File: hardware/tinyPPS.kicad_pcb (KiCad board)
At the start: 2 copper layers, 60 x 40 mm, 65 parts, among them IC1 AP2205-33Y-13, IC2 AP33772SDKZ-13-FA01, J1 USB_C_Receptacle_USB2.0_14P, J2 187-3802, J3 187-3802, J5 SM03B-SRSS-TB_LF__SN_, Q1 DMN3009SFG-7, Q2 DMN3009SFG-7, Q3 BSS123, Q4 BSS123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

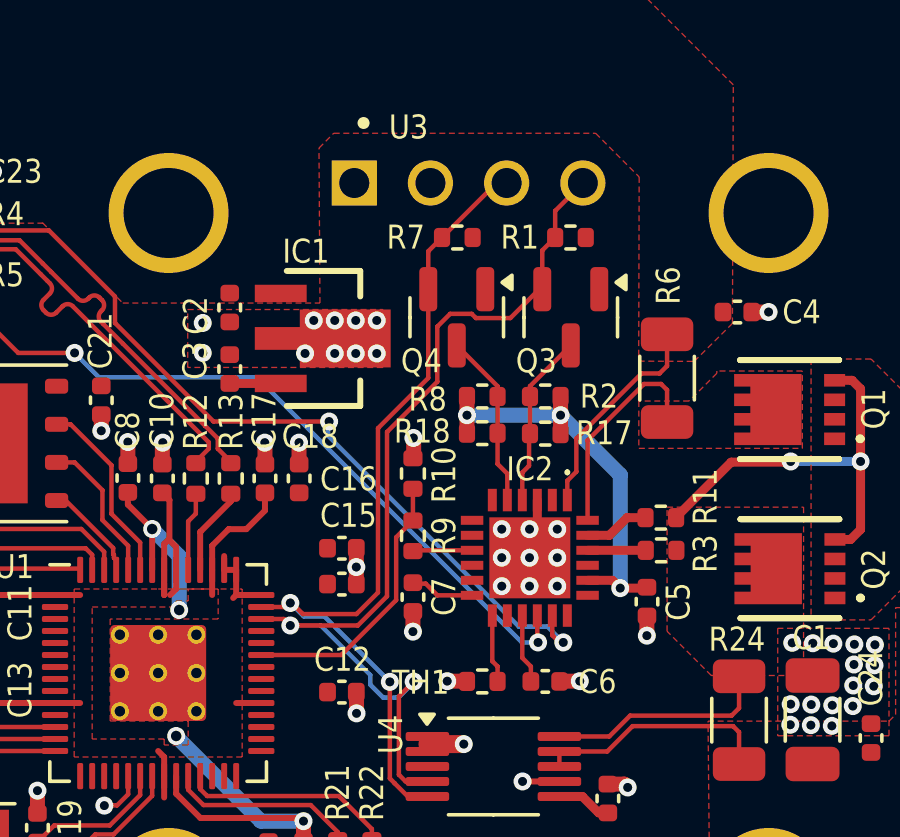
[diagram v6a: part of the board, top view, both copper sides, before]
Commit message: Schematic: Remove i2c level shifters
AP33772s' i2c can operate at 3V3, there is no need for level shifters.
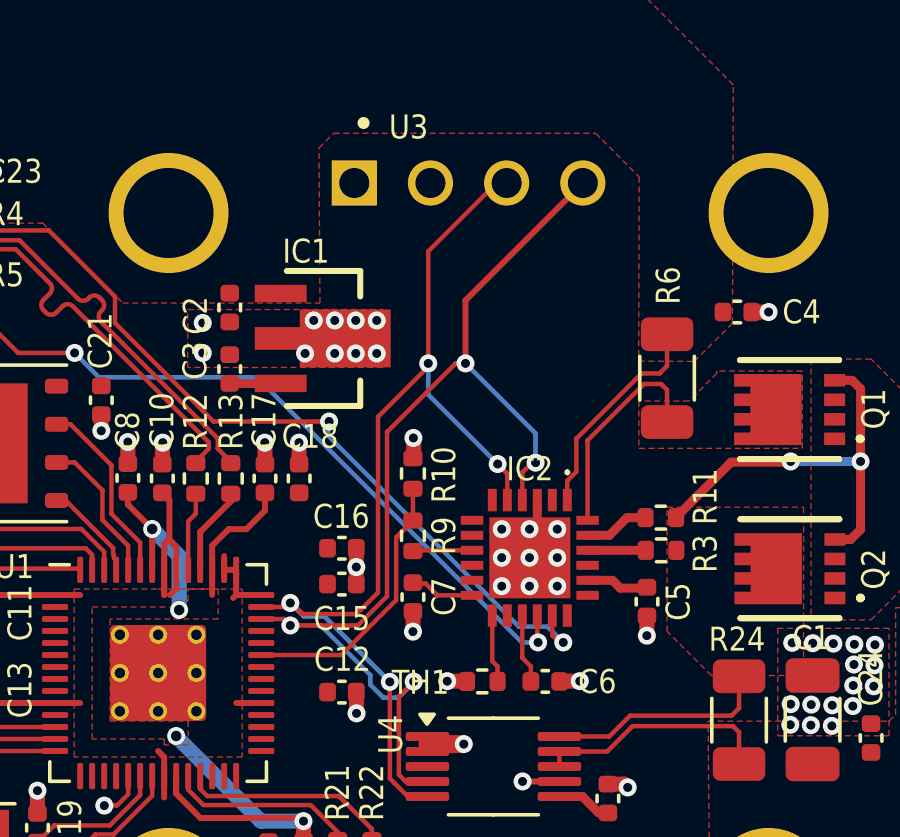
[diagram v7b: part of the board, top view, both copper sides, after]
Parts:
- removed Q3, Q4: BSS123, Package_TO_SOT_SMD:SOT-23
- removed R1, R2, R7, R8: 10k, Resistor_SMD:R_0402_1005Metric
- removed R17, R18: 4k7, Resistor_SMD:R_0402_1005Metric
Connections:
- net +5V renamed Net-(IC2-V5V)
- IC2 pad 4: /SDA_5V -> /SDA
- IC2 pad 5: /SCL_5V -> /SCL
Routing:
- net Net-(IC2-V5V): track 14.3 -> 2.09 mm, vias 3 -> 0
- net /SCL_5V: track 5.85 -> 0.00 mm
- net /SCL: track 29.1 -> 34.8 mm, vias 2 -> 4
- net /SDA_5V: track 5.53 -> 0.00 mm
- net /SDA: track 32.4 -> 37.3 mm, vias 2 -> 4

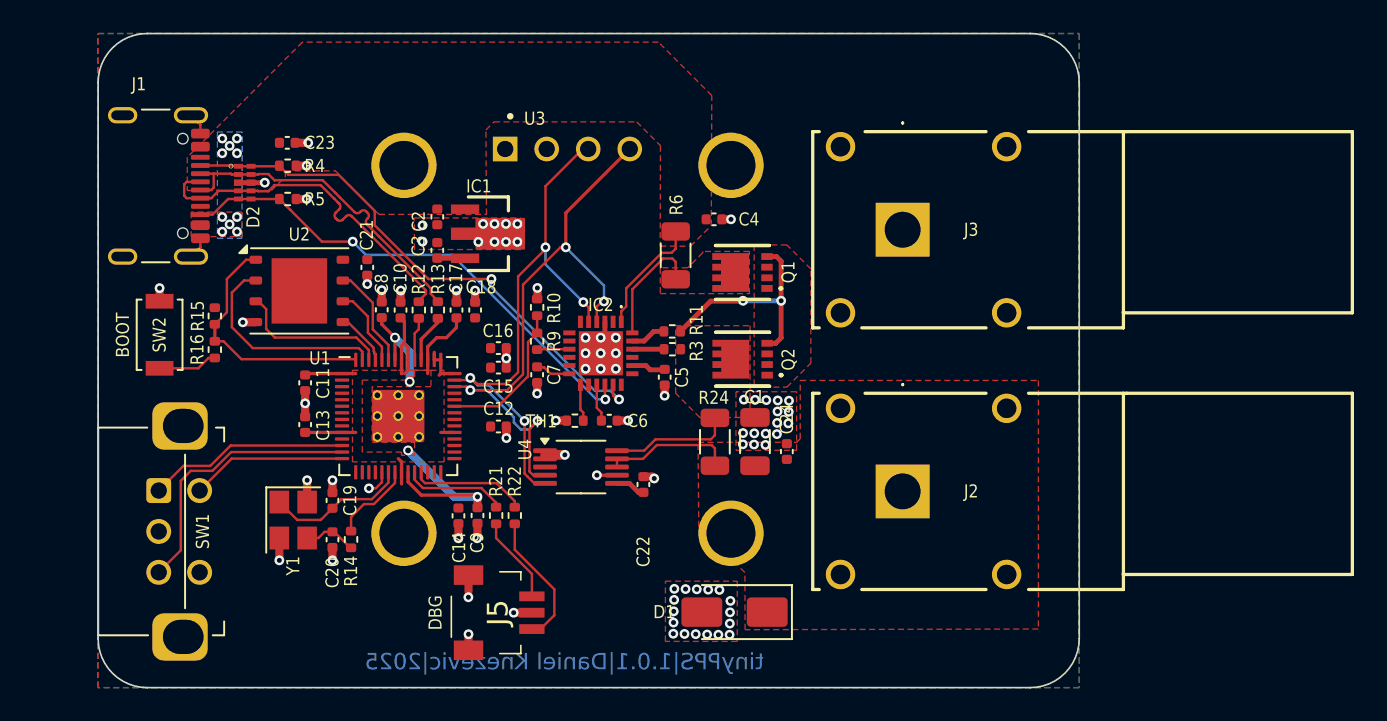
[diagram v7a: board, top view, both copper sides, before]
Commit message: PCB: Unroute PCB
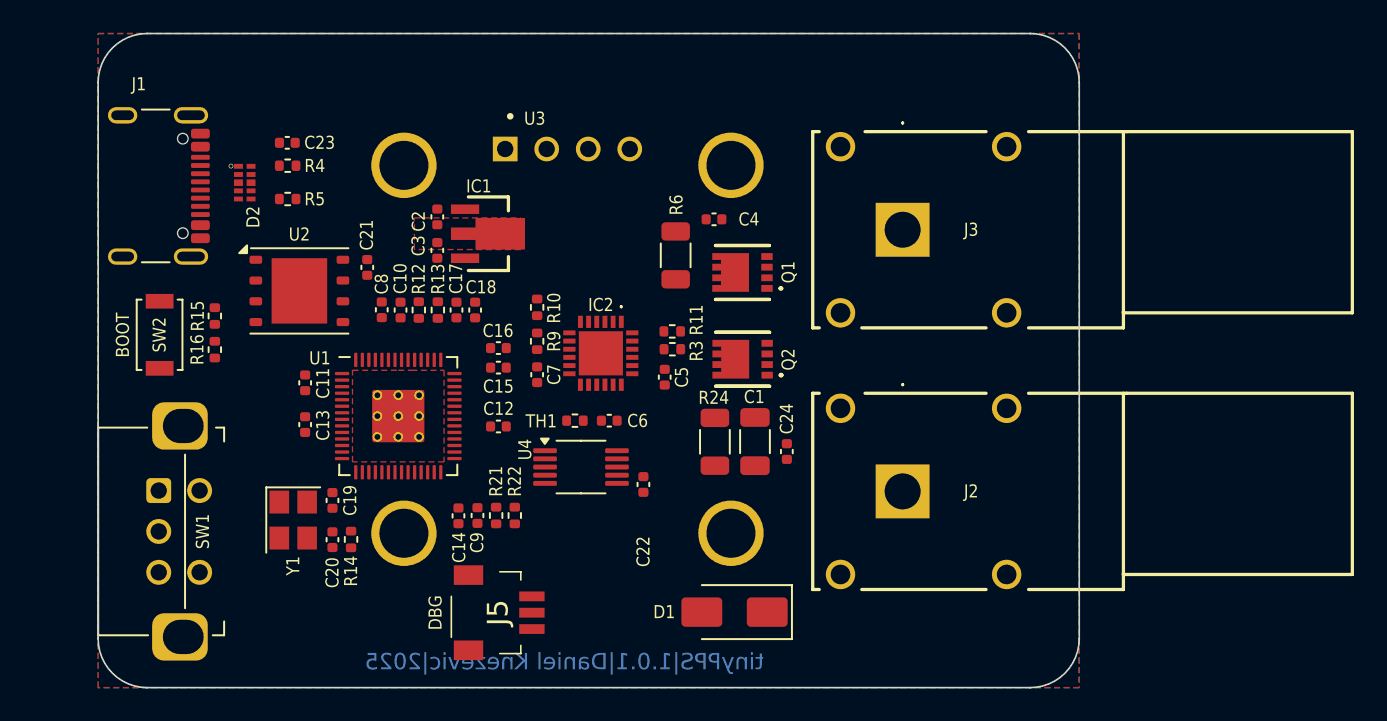
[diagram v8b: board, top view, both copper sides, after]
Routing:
- net /SDA: track 37.3 -> 0.00 mm, vias 4 -> 0
- net GND: track 35.3 -> 0.00 mm, vias 85 -> 0
- net /SCL: track 34.8 -> 0.00 mm, vias 4 -> 0
- net /CC1: track 33.4 -> 0.00 mm, vias 2 -> 0
- net /CC2: track 31.7 -> 0.00 mm, vias 2 -> 0
- net +1V1: track 21.8 -> 0.00 mm, vias 4 -> 0
- net /USB_D+: track 21.4 -> 0.00 mm
- net +3V3: track 21.0 -> 0.00 mm
- net /USB_D-: track 20.6 -> 0.00 mm
- net /GPIO10: track 16.7 -> 0.00 mm
- net /QSPI_SS: track 15.4 -> 0.00 mm
- net Net-(Q1-G): track 13.6 -> 0.00 mm, vias 2 -> 0
- net /QSPI_SD1: track 13.0 -> 0.00 mm
- net /GPIO9: track 12.4 -> 0.00 mm
- net /GPIO11: track 9.52 -> 0.00 mm
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- removed copper zone on F.Cu, net +1V1
- removed copper zone on F.Cu, net /VIN+
- removed copper zone on F.Cu, net /VOUT_PD
- removed copper zone on F.Cu, net Net-(IC2-VCC)
- removed copper zone on F.Cu, net Net-(Q1-S_1)
- removed copper zone on B.Cu, net VBUS
- removed copper zone on F.Cu, net VBUS
